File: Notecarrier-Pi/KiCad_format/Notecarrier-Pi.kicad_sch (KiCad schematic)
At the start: 10 parts

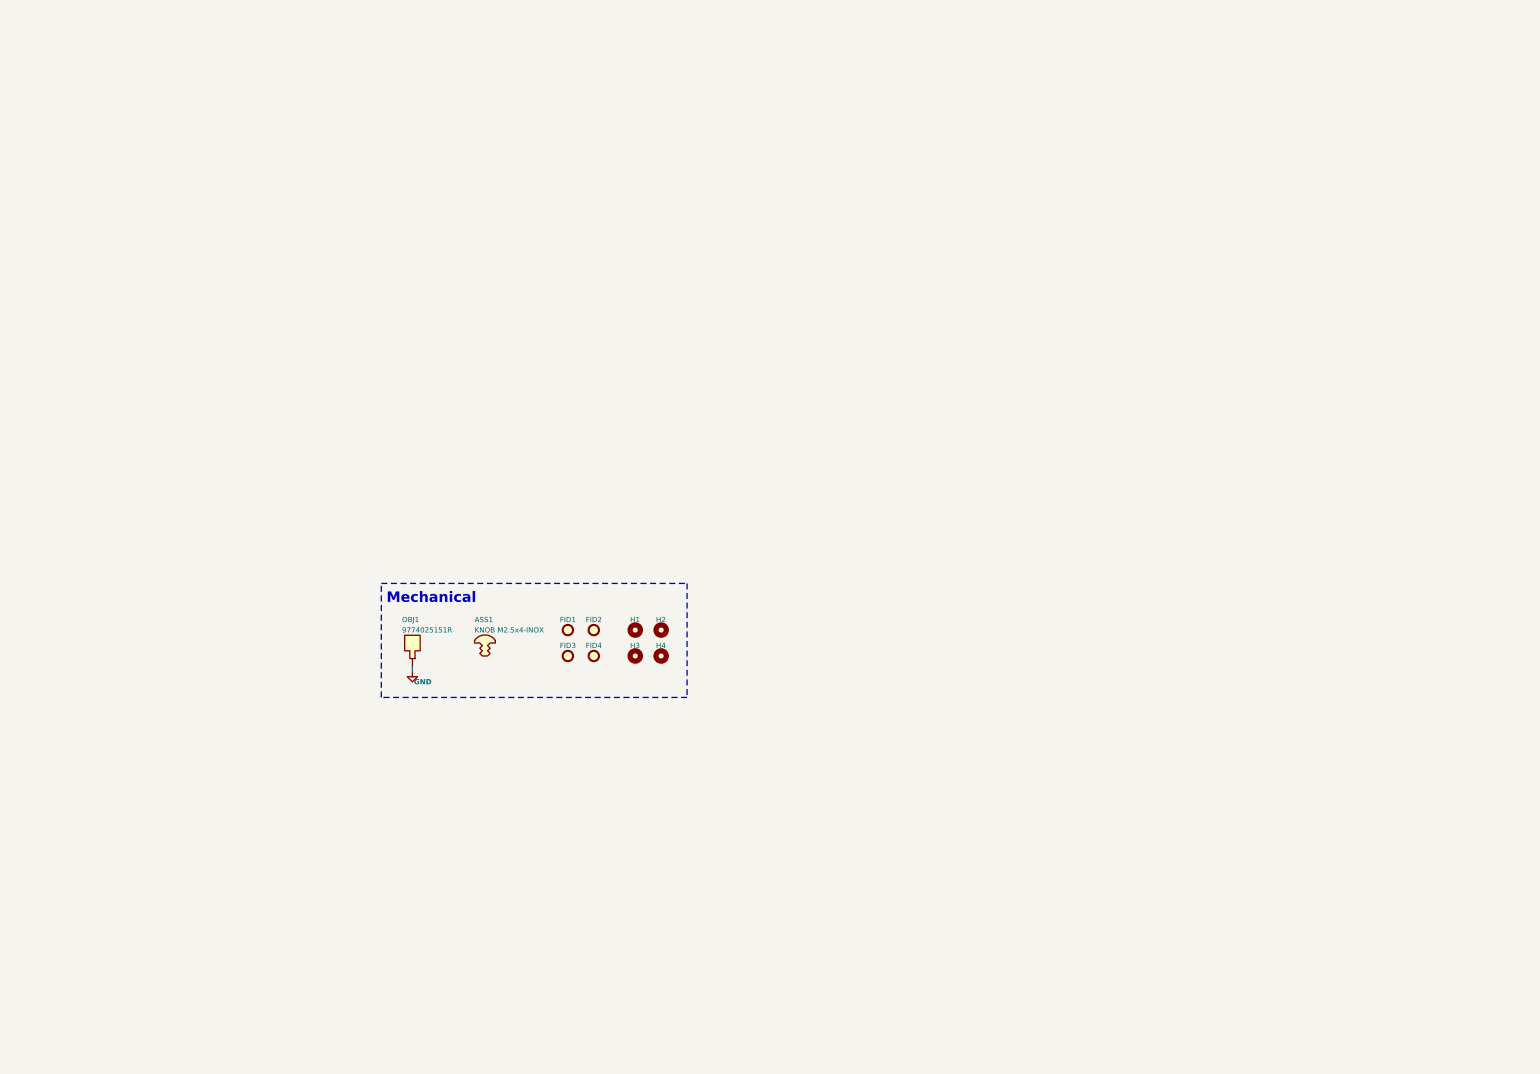
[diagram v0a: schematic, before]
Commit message: First pass port of Notecarrier-Pi schematic.
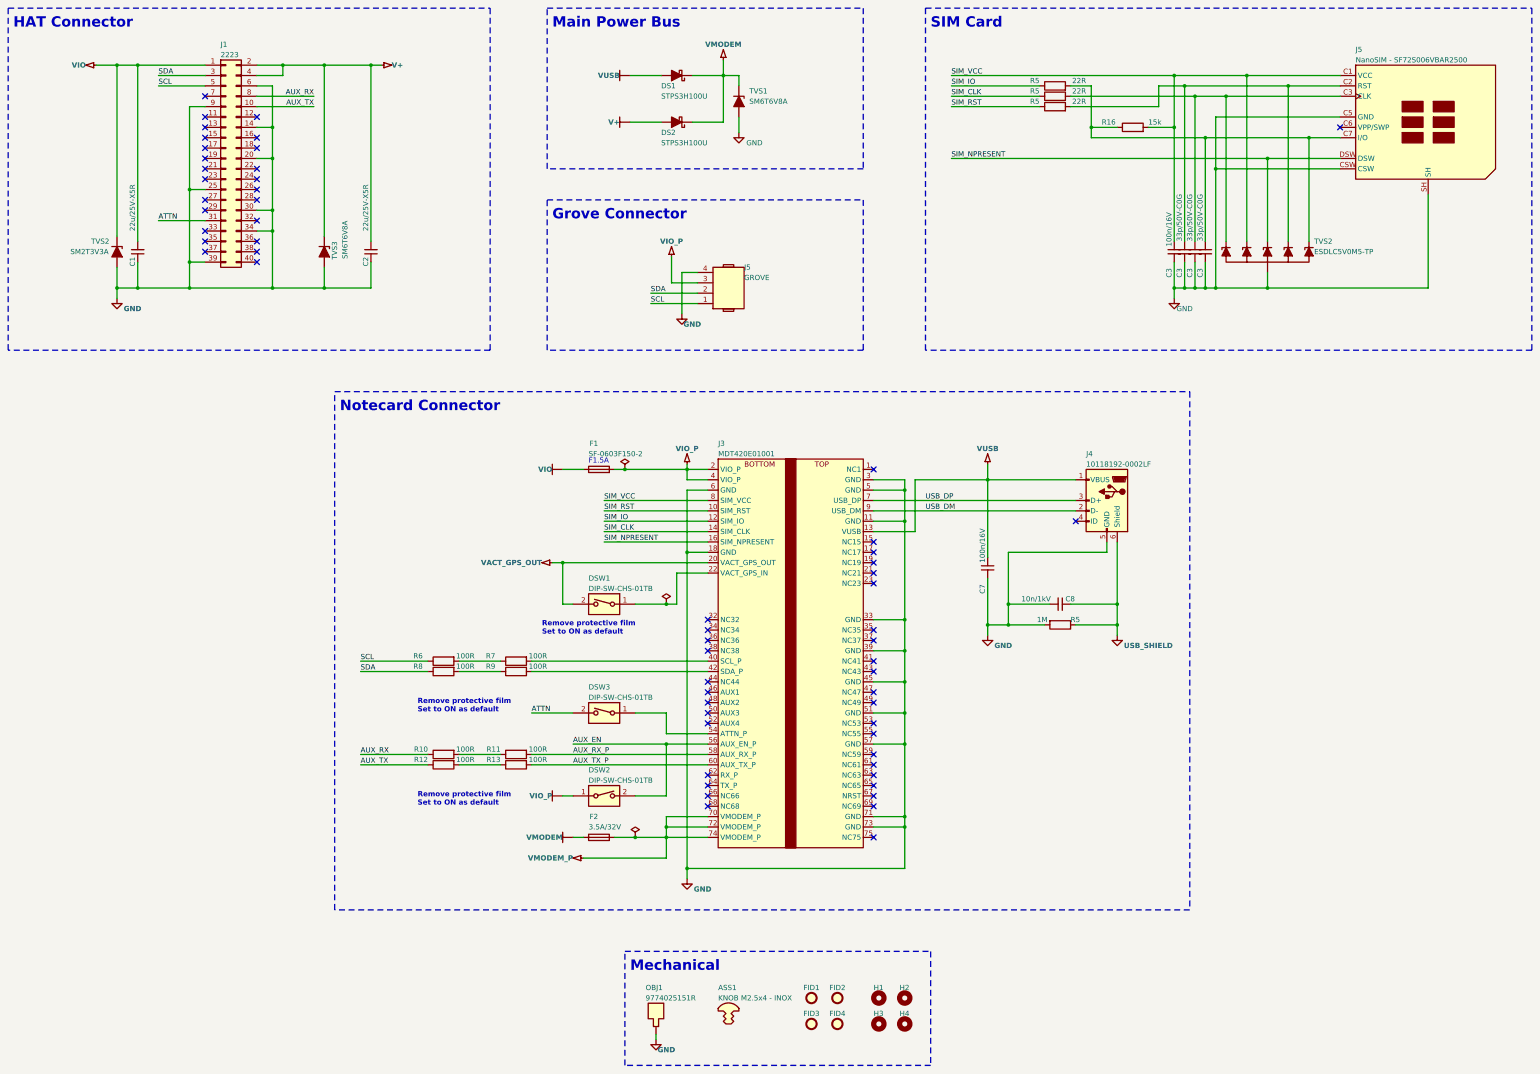
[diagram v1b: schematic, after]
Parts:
- added C1, C2: 22u/25V-X5R, blues-kicad-lib:CS-C-1206, symbol Device:C_Small
- added C3 (x3): 33p/50V-C0G, blues-kicad-lib:CS-C-0402, symbol Device:C_Small
- added C3, C7: 100n/16V, blues-kicad-lib:CS-C-0402, symbol Device:C_Small
- added C8: 10n/1kV, blues-kicad-lib:CS-C-1206, symbol Device:C_Small
- added DS1, DS2: STPS3H100U, blues-kicad-lib:SMB, symbol Device:D_Schottky_Filled
- added DSW1, DSW2, DSW3: DIP-SW-CHS-01TB, blues-kicad-lib:DSS-CHS-01TB, symbol Switch:SW_DIP_x01
- added F1: SF-0603F150-2, blues-kicad-lib:FS-0603, symbol Device:Fuse
- added F2: 3.5A/32V, blues-kicad-lib:FS-0603, symbol Device:Fuse
- added J1: 2223, symbol Connector_Generic:Conn_02x20_Odd_Even
- added J3: MDT420E01001, blues-kicad-lib:J-75-0050-MOS-M2-E, symbol blues-kicad-lib:MDT420E01001
- added J4: 10118192-0002LF, blues-kicad-lib:J-5-0065-FOS-MICROUSB10118192, symbol Connector:USB_B_Micro
- added J5: GROVE, symbol blues-kicad-lib:1125R-SMT-4P
- added J5: NanoSIM - SF72S006VBAR2500, blues-kicad-lib:J-NANOSIM-SF72S006VBA_NO-FILL, symbol blues-kicad-lib:SF72S006VBDR2500
- added R10, R11, R12, R13, R6, R7, R8, R9: 100R, blues-kicad-lib:RS-0402, symbol Device:R
- added R16: 15k, blues-kicad-lib:RS-0402, symbol Device:R
- added R5 (x3): 22R, blues-kicad-lib:RS-0603, symbol Device:R
- added R5: 1M, blues-kicad-lib:RS-1206, symbol Device:R
- added TVS1, TVS3: SM6T6V8A, blues-kicad-lib:SMB, symbol blues-kicad-lib:SM6T6V8A
- added TVS2: ESDLC5V0M5-TP, blues-kicad-lib:SOT563, symbol blues-kicad-lib:PESD5V0L5UV
- added TVS2: SM2T3V3A, blues-kicad-lib:DO214AA SMB, symbol blues-kicad-lib:SM6T6V8A
- ASS1: value KNOB M2.5x4-INOX -> KNOB M2.5x4 - INOX
- FID1, FID2, FID3, FID4: footprint blues-kicad-lib:FIDUCIAL_MIN-CLEARANCE -> blues-kicad-lib:FIDUCIAL
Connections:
- net GND: now also C1.1, C2.1, C3.2, C3.2, C3.2, C3.2, C7.2, C8.2, J1.14 (Pin_14), J1.20 (Pin_20), J1.25 (Pin_25), J1.30 (Pin_30), J1.34 (Pin_34), J1.39 (Pin_39), J1.6 (Pin_6), J1.9 (Pin_9), J3.11 (GND), J3.18 (GND), J3.3 (GND), J3.33 (GND), J3.39 (GND), J3.45 (GND), J3.5 (GND), J3.51 (GND), J3.57 (GND), J3.6 (GND), J3.71 (GND), J3.73 (GND), J4.5 (GND), J5.4, J5.C5 (GND), J5.CSW, J5.SH, R5.2, TVS1.2 (A2), TVS2.2 (A), TVS2.2 (A2), TVS3.2 (A2)
- new net: C3.1, J5.C2 (RST), R5.2, TVS2.5 (K4)
- new net: C3.1, J5.C7 (I/O), R16.1, R5.2, TVS2.6 (K5)
- new net: R12.2, R13.1
- new net: R6.2, R7.1
- new net: R8.2, R9.1
- new net: J3.42 (SDA_P), R9.2
- new net: C3.1, J5.C3 (CLK), R5.2, TVS2.1 (K1)
- new net: C8.1, J4.6 (Shield), R5.1
- new net: R10.2, R11.1
- new net: DSW1.1, J3.22 (VACT_GPS_IN)
- new net: J3.40 (SCL_P), R7.2
- new net: DSW3.1, J3.54 (ATTN_P)
- new net ATTN: DSW3.2, J1.31 (Pin_31)
- new net AUX_EN: DSW2.2, J3.56 (AUX_EN_P)
- new net AUX_RX: J1.8 (Pin_8), R10.1
- new net AUX_RX_P: J3.58 (AUX_RX_P), R11.2
- new net AUX_TX: J1.10 (Pin_10), R12.1
- new net AUX_TX_P: J3.60 (AUX_TX_P), R13.2
- new net SCL: J1.5 (Pin_5), J5.1, R6.1
- new net SDA: J1.3 (Pin_3), J5.2, R8.1
- new net SIM_CLK: J3.14 (SIM_CLK), R5.1
- new net SIM_IO: J3.12 (SIM_IO), R5.1
- new net SIM_NPRESENT: J3.16 (SIM_NPRESENT), J5.DSW, TVS2.4 (K3)
- new net SIM_RST: J3.10 (SIM_RST), R5.1
- new net SIM_VCC: C3.1, J3.8 (SIM_VCC), J5.C1 (VCC), R16.2, TVS2.3 (K2)
- new net USB_DM: J3.9 (USB_DM), J4.2 (D-)
- new net USB_DP: J3.7 (USB_DP), J4.3 (D+)
- new net V+: C2.2, DS2.2 (A), J1.2 (Pin_2), J1.4 (Pin_4), TVS3.1 (A1)
- new net VACT_GPS_OUT: DSW1.2, J3.20 (VACT_GPS_OUT)
- new net VIO: C1.2, DSW2.1, F1.1, J1.1 (Pin_1), TVS2.1 (A1)
- new net VIO_P: F1.2, J3.2 (VIO_P), J3.4 (VIO_P), J5.3
- new net VMODEM: DS1.1 (K), DS2.1 (K), F2.1, TVS1.1 (A1)
- new net VMODEM_P: F2.2, J3.70 (VMODEM_P), J3.72 (VMODEM_P), J3.74 (VMODEM_P)
- new net VUSB: C7.1, DS1.2 (A), J3.13 (VUSB), J4.1 (VBUS)
- no-connect marks 0 -> 60
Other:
- note added: "F1.5A"
- note added: "Grove Connector"
- note added: "HAT Connector"
- note added: "Main Power Bus"
- note added: "Notecard Connector"
- note added: "Remove protective film Set to ON as default"
- note added: "SIM Card"
- moved on the sheet: ASS1, FID1, FID2, FID3, FID4, H1, H2, H3, H4, OBJ1

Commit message: Port fab, silk and copper layers for Notecarrier-Pi.
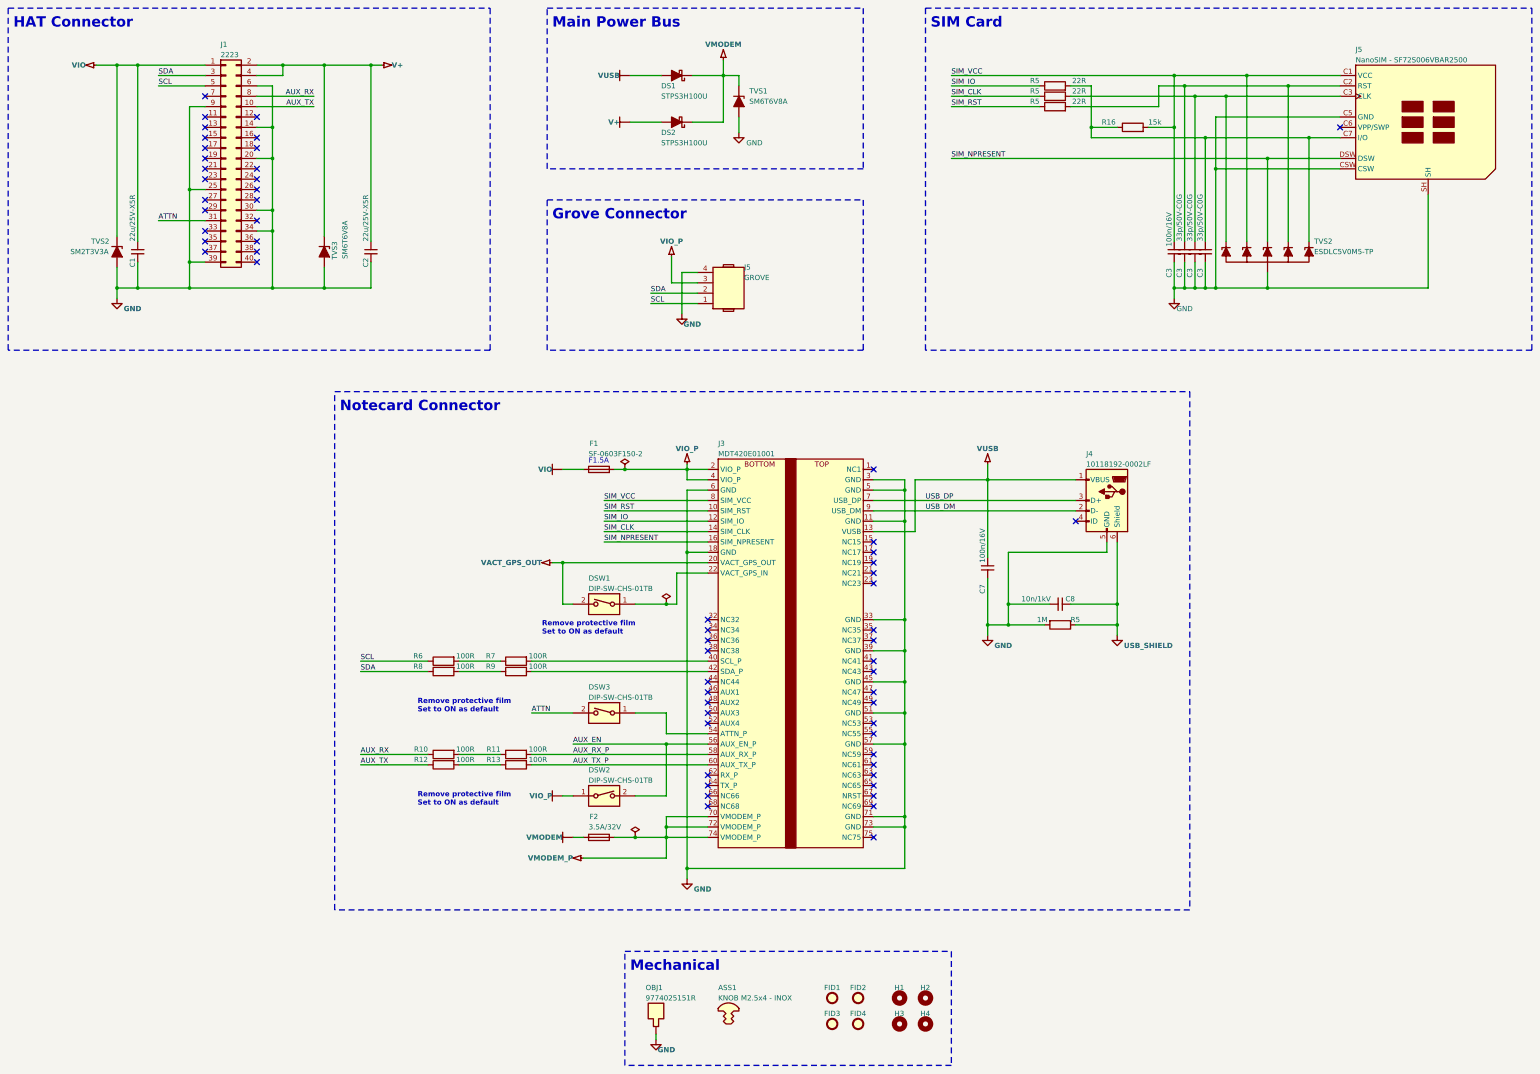
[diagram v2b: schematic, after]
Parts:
- H1, H2, H3, H4: footprint blues-kicad-lib:FORO-0330-U -> blues-kicad-lib:FORO-0270-U
- J1: footprint (none) -> blues-kicad-lib:J-20x2-0254-FDT-SSQX03
- J5: footprint (none) -> blues-kicad-lib:J-4-0200-MOS-GROVE_NO-SILK
- TVS2: footprint blues-kicad-lib:DO214AA SMB -> blues-kicad-lib:D-DO216AA_NO-SILK
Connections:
- net GND: now also C1.2, C2.2; no longer C1.1, C2.1
- net V+: now also C2.1; no longer C2.2
- net VIO: now also C1.1; no longer C1.2
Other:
- moved on the sheet: C1, C2, FID1, FID2, FID3, FID4, H1, H2, H3, H4

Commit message: Create rules and clearances to suit Notecarrier-Pi port.
Also, fix VIO_P power symbol which had VIO net name.
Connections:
- net VIO: no longer DSW2.1
- net VIO_P: now also DSW2.1
